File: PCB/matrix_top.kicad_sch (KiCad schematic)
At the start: 64 parts, among them J23 Conn_02x02_Top_Bottom, J24 Conn_02x02_Top_Bottom, J25 Conn_02x02_Top_Bottom, J30 Conn_01x04, J31 Conn_01x04, J32 Conn_01x04

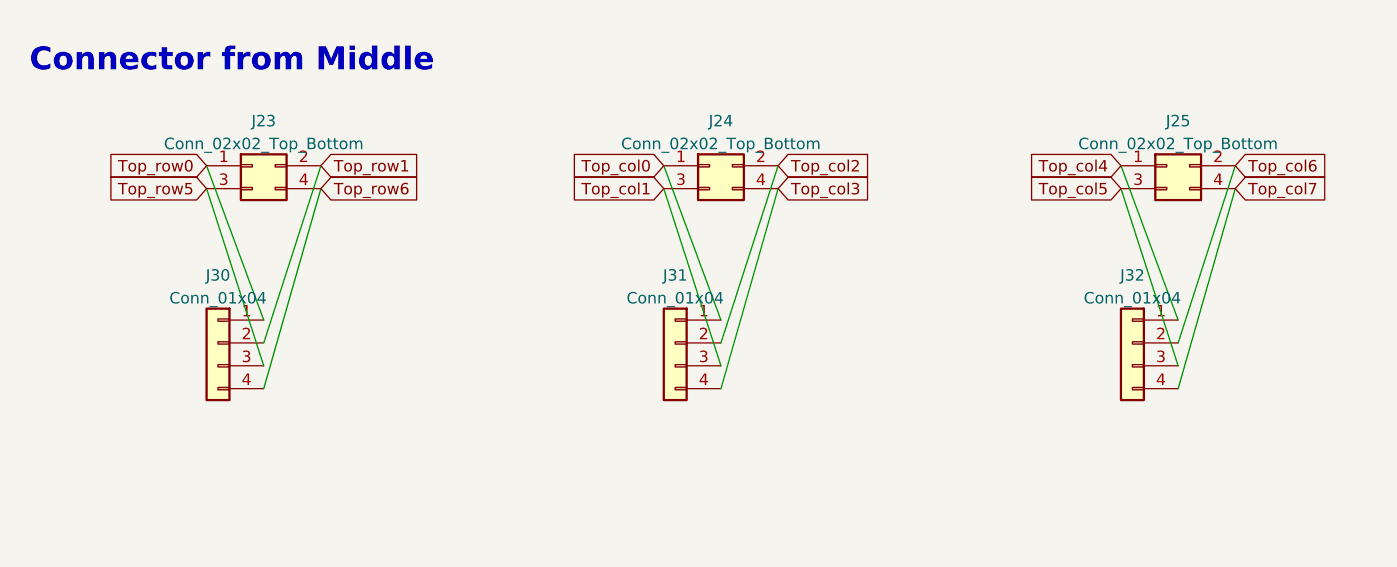
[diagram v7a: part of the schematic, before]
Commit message: 3枚の基板を1枚にまとめ中
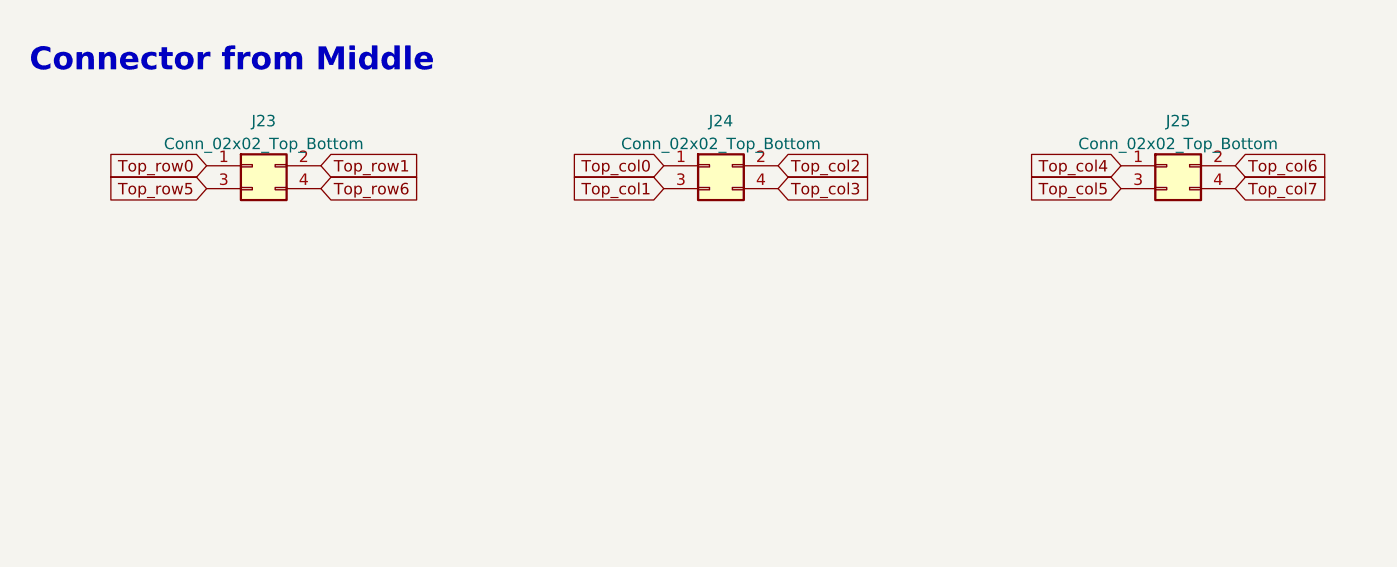
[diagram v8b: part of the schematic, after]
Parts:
- removed J30, J31, J32: Conn_01x04, Connector_PinHeader_2.54mm:PinHeader_1x04_P2.54mm_Vertical, symbol Connector_Generic:Conn_01x04
- J23, J24, J25: footprint Connector_JST:JST_SH_SM04B-SRSS-TB_1x04-1MP_P1.00mm_Horizontal -> locallib:JST_SH_SM04B-SRSS-TB_1x04-1MP_P1.00mm_Horizontal_wCable_housing_spare_pin
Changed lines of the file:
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@@
-    (stroke (width 0) (type default) (color 0 0 0 0))
-  )
-  (wire (pts (xy 34.925 134.62) (xy 41.275 154.305))
     (stroke (width 0) (type default) (color 0 0 0 0))
   )
@@
     (stroke (width 0) (type default) (color 0 0 0 0))
   )
-  (wire (pts (xy 149.225 134.62) (xy 142.875 156.845))
-    (stroke (width 0) (type default) (color 0 0 0 0))
-  )
   (wire (pts (xy 71.12 58.42) (xy 71.12 105.41))
     (stroke (width 0) (type default) (color 0 0 0 0))
@@
     (stroke (width 0) (type default) (color 0 0 0 0))
   )
-  (wire (pts (xy 92.075 149.225) (xy 85.725 132.08))
-    (stroke (width 0) (type default) (color 0 0 0 0))
-  )
   (wire (pts (xy 153.67 46.99) (xy 137.16 46.99))
     (stroke (width 0) (type default) (color 0 0 0 0))
@@
     (stroke (width 0) (type default) (color 0 0 0 0))
   )
-  (wire (pts (xy 98.425 132.08) (xy 92.075 151.765))
-    (stroke (width 0) (type default) (color 0 0 0 0))
-  )
   (wire (pts (xy 38.1 46.99) (xy 38.1 58.42))
     (stroke (width 0) (type default) (color 0 0 0 0))
@@
     (stroke (width 0) (type default) (color 0 0 0 0))
   )
-  (wire (pts (xy 47.625 132.08) (xy 41.275 151.765))
-    (stroke (width 0) (type default) (color 0 0 0 0))
-  )
   (wire (pts (xy 163.83 97.79) (xy 163.83 101.6))
     (stroke (width 0) (type default) (color 0 0 0 0))
@@
     (stroke (width 0) (type default) (color 0 0 0 0))
   )
-  (wire (pts (xy 41.275 149.225) (xy 34.925 132.08))
-    (stroke (width 0) (type default) (color 0 0 0 0))
-  )
-  (wire (pts (xy 136.525 134.62) (xy 142.875 154.305))
-    (stroke (width 0) (type default) (color 0 0 0 0))
-  )
   (wire (pts (xy 97.79 66.04) (xy 97.79 69.85))
     (stroke (width 0) (type default) (color 0 0 0 0))
@@
     (stroke (width 0) (type default) (color 0 0 0 0))
   )
-  (wire (pts (xy 41.275 156.845) (xy 47.625 134.62))
-    (stroke (width 0) (type default) (color 0 0 0 0))
-  )
   (wire (pts (xy 114.3 66.04) (xy 114.3 67.31))
     (stroke (width 0) (type default) (color 0 0 0 0))
@@
     (stroke (width 0) (type default) (color 0 0 0 0))
   )
-  (wire (pts (xy 92.075 154.305) (xy 85.725 134.62))
-    (stroke (width 0) (type default) (color 0 0 0 0))
-  )
   (wire (pts (xy 252.73 46.99) (xy 252.73 58.42))
     (stroke (width 0) (type default) (color 0 0 0 0))
@@
     (stroke (width 0) (type default) (color 0 0 0 0))
   )
-  (wire (pts (xy 98.425 134.62) (xy 92.075 156.845))
-    (stroke (width 0) (type default) (color 0 0 0 0))
-  )
   (wire (pts (xy 34.925 99.06) (xy 147.32 99.06))
     (stroke (width 0) (type default) (color 0 0 0 0))
@@
     (stroke (width 0) (type default) (color 0 0 0 0))
   )
-  (wire (pts (xy 142.875 151.765) (xy 149.225 132.08))
-    (stroke (width 0) (type default) (color 0 0 0 0))
-  )
   (wire (pts (xy 48.26 66.04) (xy 48.26 67.31))
     (stroke (width 0) (type default) (color 0 0 0 0))
@@
   )
   (wire (pts (xy 34.925 101.6) (xy 130.81 101.6))
-    (stroke (width 0) (type default) (color 0 0 0 0))
-  )
-  (wire (pts (xy 136.525 132.08) (xy 142.875 149.225))
     (stroke (width 0) (type default) (color 0 0 0 0))
   )
@@
     (property "Reference" "J24" (id 0) (at 92.075 127.1102 0))
     (property "Value" "Conn_02x02_Top_Bottom" (id 1) (at 92.075 129.6471 0))
-    (property "Footprint" "Connector_JST:JST_SH_SM04B-SRSS-TB_1x04-1MP_P1.00mm_Horizontal" (id 2) (at 90.805 132.08 0)
+    (property "Footprint" "locallib:JST_SH_SM04B-SRSS-TB_1x04-1MP_P1.00mm_Horizontal_wCable_housing_spare_pin" (id 2) (at 90.805 132.08 0)
       (effects (font (size 1.27 1.27)) hide)
     )
@@
     )
   )
-  (symbol (lib_id "Connector_Generic:Conn_01x04") (at 137.795 151.765 0) (mirror y) (unit 1)
-    (in_bom yes) (on_board yes) (fields_autoplaced)
-    (property "Reference" "J32" (id 0) (at 137.795 144.2552 0))
-    (property "Value" "Conn_01x04" (id 1) (at 137.795 146.7921 0))
-    (property "Footprint" "Connector_PinHeader_2.54mm:PinHeader_1x04_P2.54mm_Vertical" (id 2) (at 137.795 151.765 0)
-      (effects (font (size 1.27 1.27)) hide)
-    )
-    (property "Datasheet" "~" (id 3) (at 137.795 151.765 0)
-      (effects (font (size 1.27 1.27)) hide)
-    )
-    (pin "1")
-    (pin "2")
-    (pin "3")
-    (pin "4")
-  )
   (symbol (lib_id "Connector_Generic:Conn_01x01") (at 170.18 110.49 270) (unit 1)
     (in_bom yes) (on_board yes)
@@
     (pin "2")
   )
-  (symbol (lib_id "Connector_Generic:Conn_01x04") (at 86.995 151.765 0) (mirror y) (unit 1)
-    (in_bom yes) (on_board yes) (fields_autoplaced)
-    (property "Reference" "J31" (id 0) (at 86.995 144.2552 0))
-    (property "Value" "Conn_01x04" (id 1) (at 86.995 146.7921 0))
-    (property "Footprint" "Connector_PinHeader_2.54mm:PinHeader_1x04_P2.54mm_Vertical" (id 2) (at 86.995 151.765 0)
-      (effects (font (size 1.27 1.27)) hide)
-    )
-    (property "Datasheet" "~" (id 3) (at 86.995 151.765 0)
-      (effects (font (size 1.27 1.27)) hide)
-    )
-    (pin "1")
-    (pin "2")
-    (pin "3")
-    (pin "4")
-  )
   (symbol (lib_id "Connector_Generic:Conn_01x01") (at 137.16 110.49 270) (unit 1)
     (in_bom yes) (on_board yes)
@@
     (pin "1")
     (pin "2")
-  )
-  (symbol (lib_id "Connector_Generic:Conn_01x04") (at 36.195 151.765 0) (mirror y) (unit 1)
-    (in_bom yes) (on_board yes) (fields_autoplaced)
-    (property "Reference" "J30" (id 0) (at 36.195 144.2552 0))
-    (property "Value" "Conn_01x04" (id 1) (at 36.195 146.7921 0))
-    (property "Footprint" "Connector_PinHeader_2.54mm:PinHeader_1x04_P2.54mm_Vertical" (id 2) (at 36.195 151.765 0)
-      (effects (font (size 1.27 1.27)) hide)
-    )
-    (property "Datasheet" "~" (id 3) (at 36.195 151.765 0)
-      (effects (font (size 1.27 1.27)) hide)
-    )
-    (pin "1")
-    (pin "2")
-    (pin "3")
-    (pin "4")
   )
   (symbol (lib_id "Switch:SW_Push") (at 125.73 90.17 0) (unit 1)
@@
     (property "Reference" "J23" (id 0) (at 41.275 127.1102 0))
     (property "Value" "Conn_02x02_Top_Bottom" (id 1) (at 41.275 129.6471 0))
-    (property "Footprint" "Connector_JST:JST_SH_SM04B-SRSS-TB_1x04-1MP_P1.00mm_Horizontal" (id 2) (at 40.005 132.08 0)
+    (property "Footprint" "locallib:JST_SH_SM04B-SRSS-TB_1x04-1MP_P1.00mm_Horizontal_wCable_housing_spare_pin" (id 2) (at 40.005 132.08 0)
       (effects (font (size 1.27 1.27)) hide)
     )
@@
     (property "Reference" "J25" (id 0) (at 142.875 127.1102 0))
     (property "Value" "Conn_02x02_Top_Bottom" (id 1) (at 142.875 129.6471 0))
-    (property "Footprint" "Connector_JST:JST_SH_SM04B-SRSS-TB_1x04-1MP_P1.00mm_Horizontal" (id 2) (at 141.605 132.08 0)
-      (effects (font (size 1.27 1.27)) hide)
-    )
+    (property "Footprint" "locallib:JST_SH_SM04B-SRSS-TB_1x04-1MP_P1.00mm_Horizontal_wCable_housing_spare_pin" (id 2) (at 141.605 132.08 0)
+      (effects (font (size 1.27 1.27)) hide)
+    )
